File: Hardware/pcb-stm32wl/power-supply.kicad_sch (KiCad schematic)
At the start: 38 parts, among them J1 S1001-46R, J2 JST-PH, J3 S1001-46R, J4 RF_Shield_One_Piece, J5 S1001-46R, J6 S1001-46R, Q1 PMV32UP,215, U1 TPS22917DBV, U2 TPS3839G18DBZT‎, U3 TPS22917DBV, U4 RP605Z283B

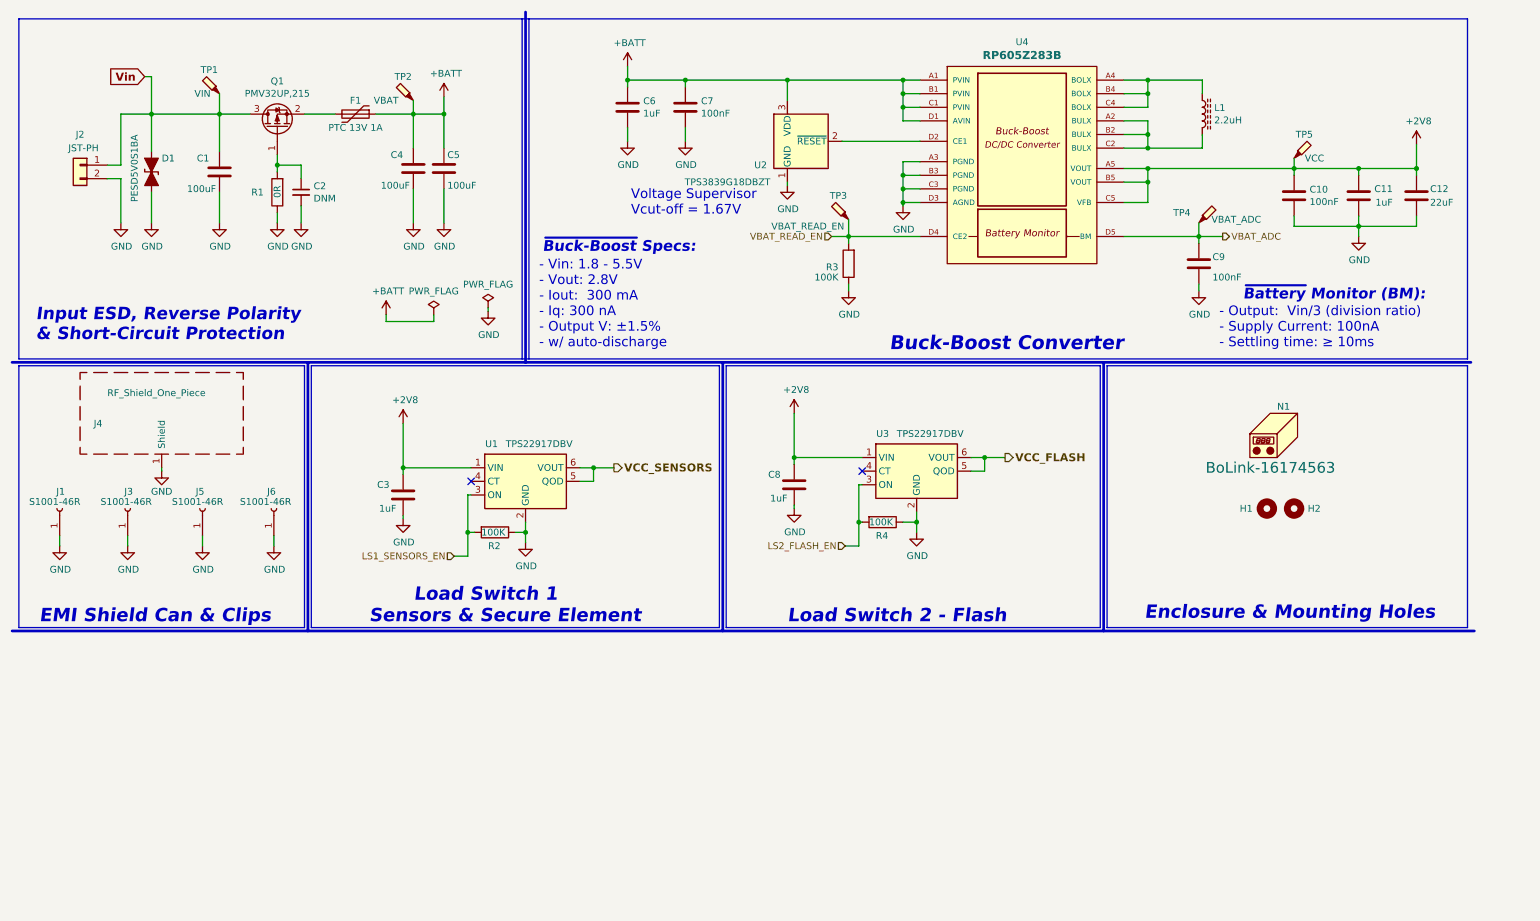
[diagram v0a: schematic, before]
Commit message: updated strain gauge connections and created todo tasks
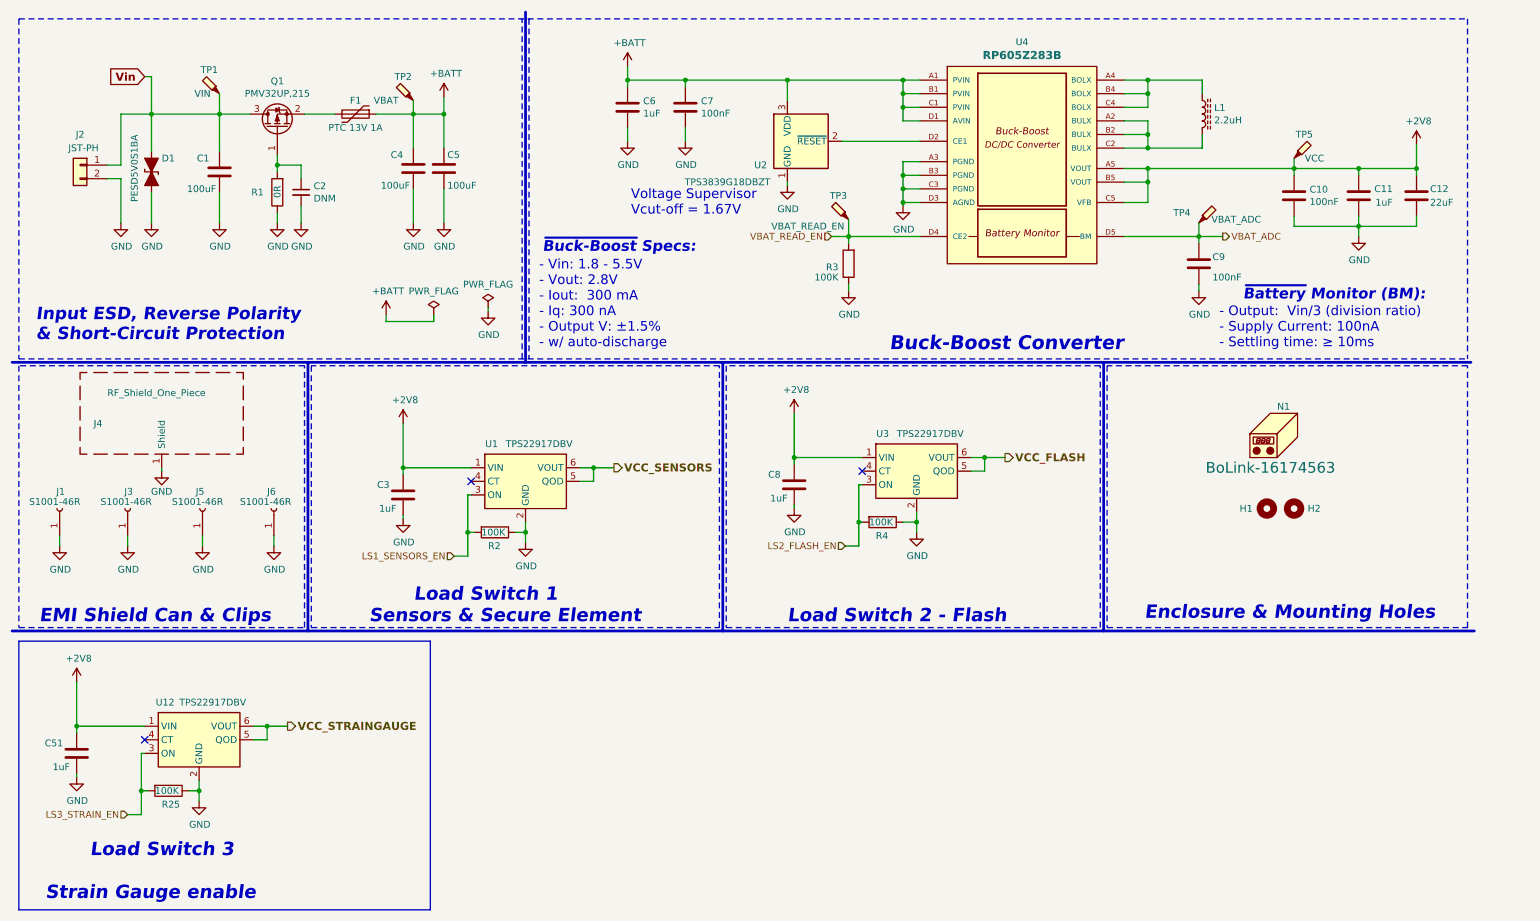
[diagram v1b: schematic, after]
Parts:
- added C51: 1uF, Capacitor_SMD:C_0402_1005Metric, symbol Device:C
- added R25: 100K, Resistor_SMD:R_0402_1005Metric, symbol Device:R
- added U12: TPS22917DBV, Package_TO_SOT_SMD:SOT-23-6, symbol Power_Management:TPS22917DBV
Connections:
- net +2V8: now also C51.1, U12.1 (VIN)
- net GND: now also C51.2, R25.1, U12.2 (GND)
- new net LS3_STRAIN_EN: R25.2, U12.3 (ON)
- new net VCC_STRAINGAUGE: U12.5 (QOD), U12.6 (VOUT)
- no-connect marks 2 -> 3
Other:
- note added: "Load Switch 3 Strain Gauge enable"

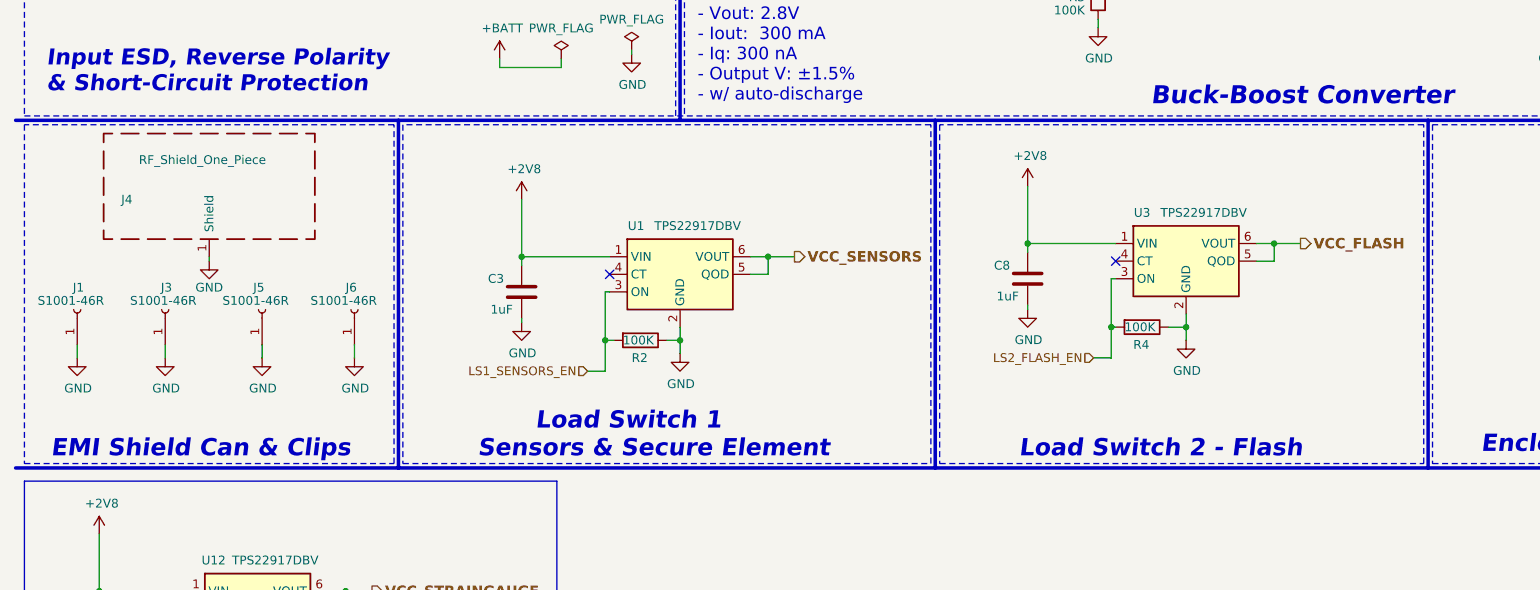
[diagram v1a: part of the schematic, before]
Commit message: deleted some components today, finished selecting BUCK converter components for 5V
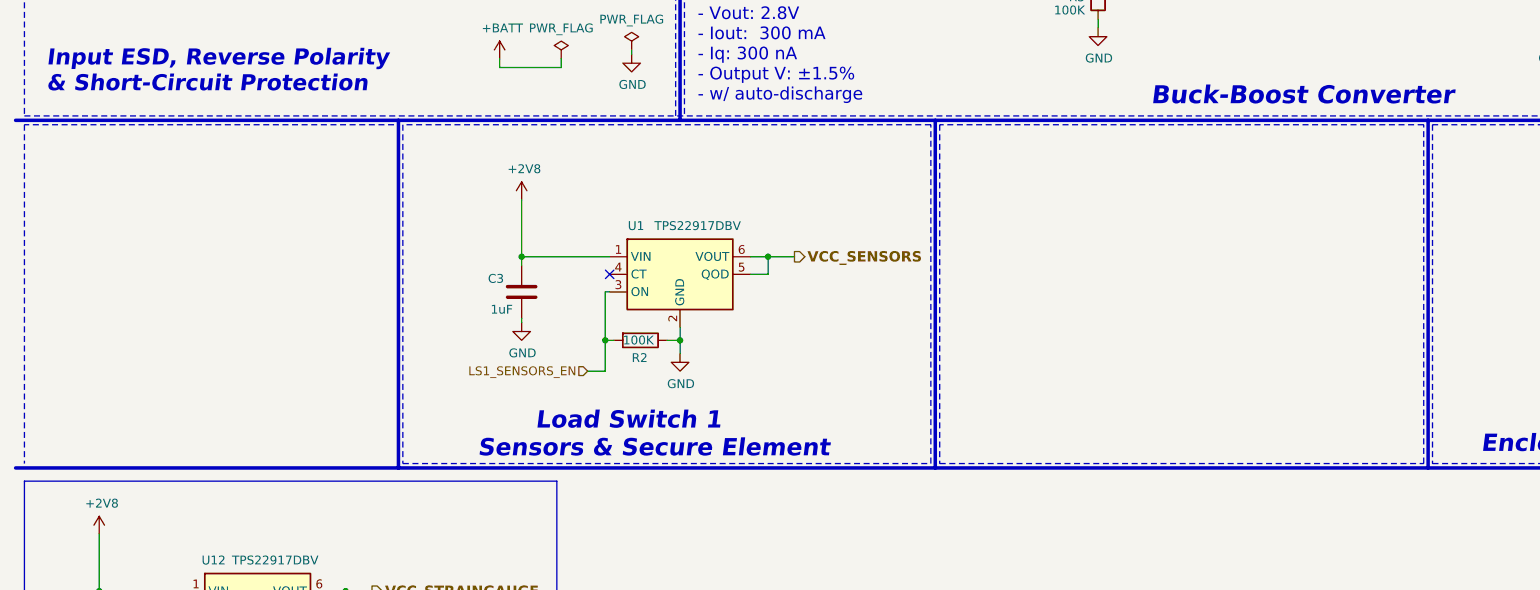
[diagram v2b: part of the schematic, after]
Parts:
- removed C8: 1uF, Capacitor_SMD:C_0402_1005Metric, symbol Device:C
- removed J1, J3, J5, J6: S1001-46R, node-lib-v1:RF_Shield_Clip_S1001-46R, symbol Connector:Conn_01x01_Female
- removed J4: RF_Shield_One_Piece, node-lib-v1:RF_Shield_SnapOn_30x20mm_w_Cutout_n_GND_Pads, symbol Device:RF_Shield_One_Piece
- removed R4: 100K, Resistor_SMD:R_0402_1005Metric, symbol Device:R
- removed U3: TPS22917DBV, Package_TO_SOT_SMD:SOT-23-6, symbol Power_Management:TPS22917DBV
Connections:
- no-connect marks 3 -> 2
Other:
- note removed: "EMI Shield Can & Clips"
- note removed: "Load Switch 2 - Flash"
